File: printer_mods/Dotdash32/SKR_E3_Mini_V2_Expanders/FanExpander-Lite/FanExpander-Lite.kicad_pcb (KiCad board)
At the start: 2 copper layers, 35.1 x 34.7 mm, 31 parts, among them J1 FAN1, J2 FAN2, J3 FAN3, J4 FAN4, J5 EXP1_IN, J6 FAN1_IN, J7 IO_PassThrough, Q1 IRLML6344, Q2 IRLML6344, Q3 IRLML6344

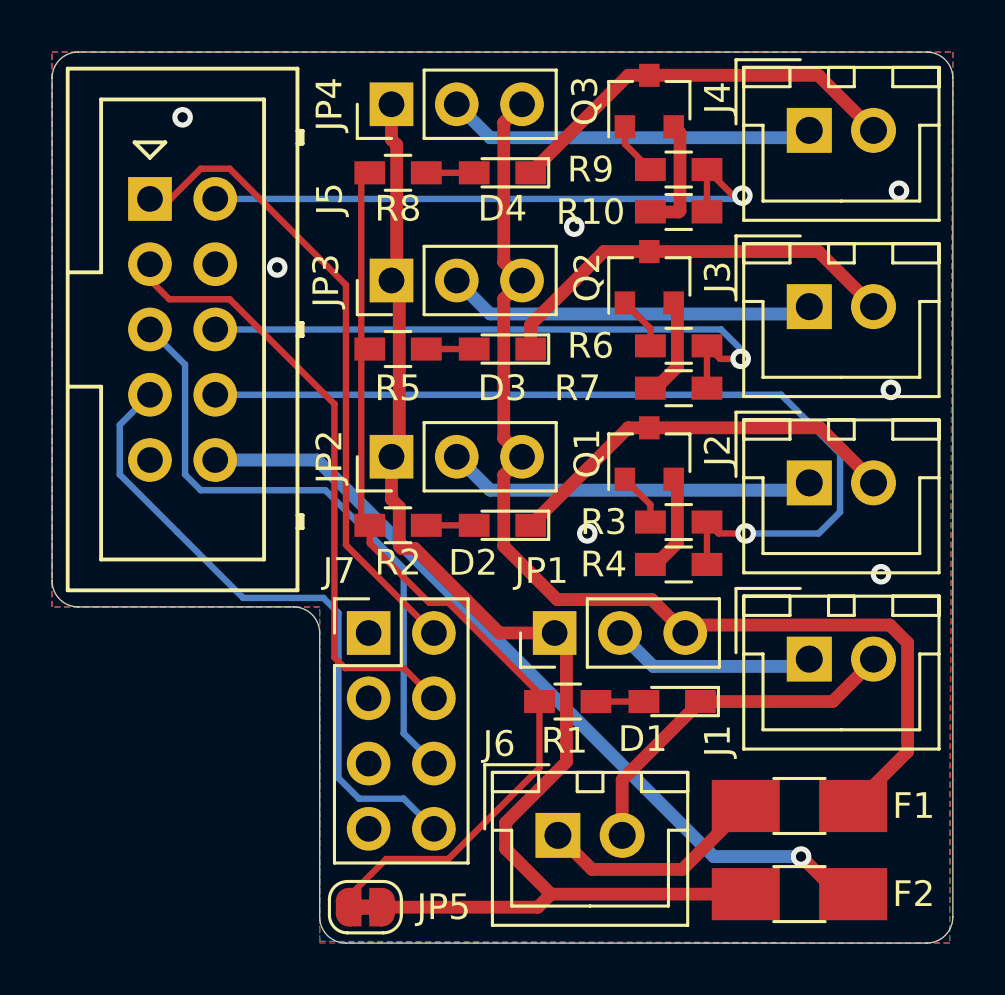
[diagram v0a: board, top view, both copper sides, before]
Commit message: feat: redo layout to use backside SMD parts
move to align with main board version, compactness!
Also moving to larger THT PTC fuses
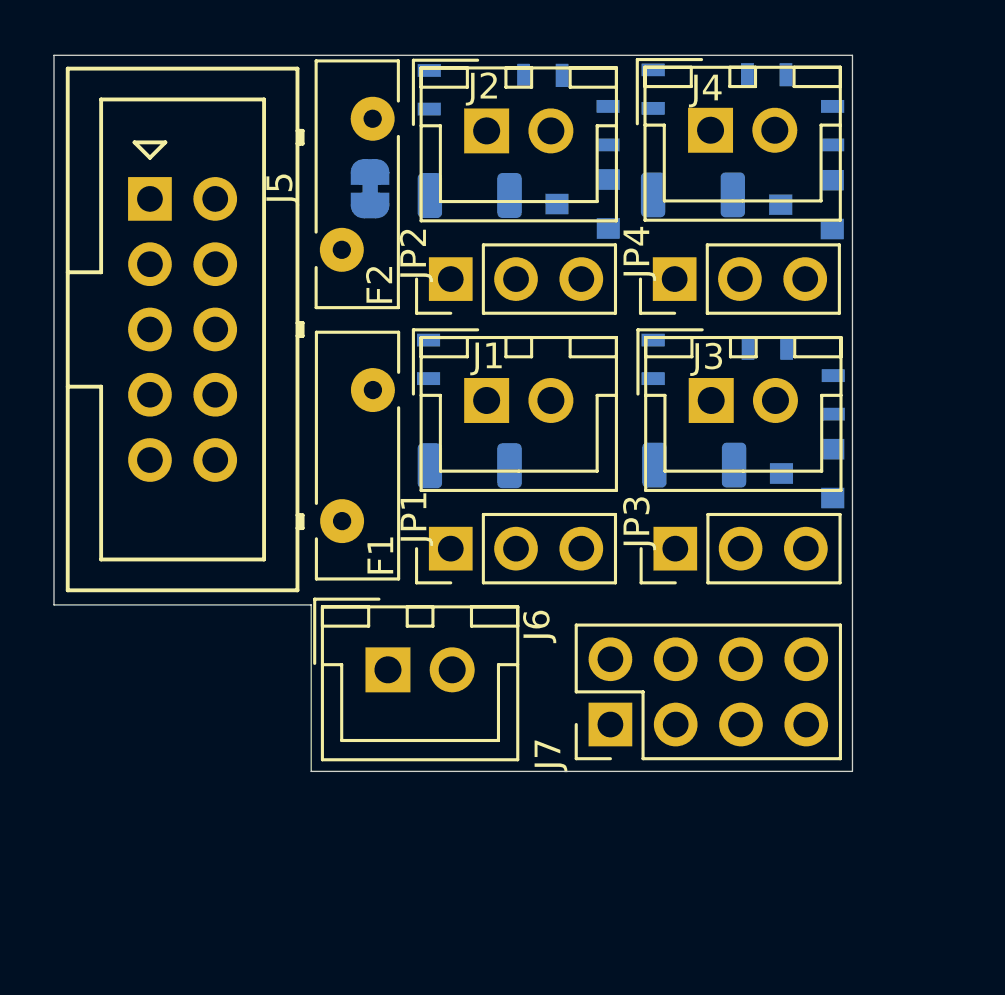
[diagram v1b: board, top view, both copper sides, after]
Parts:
- D1, D2, D3, D4: footprint LEDs:LED_0603_HandSoldering -> LED_SMD:LED_1206_3216Metric_ReverseMount_Hole1.8x2.4mm; moved to B.Cu
- F1: value Polyfuse-2A -> Polyfuse-3A; footprint Fuse_Holders_and_Fuses:Fuse_SMD1206_HandSoldering -> Fuse:Fuse_Bourns_MF-RHT200
- F2: footprint Fuse_Holders_and_Fuses:Fuse_SMD1206_HandSoldering -> Fuse:Fuse_Bourns_MF-RHT200
- JP5, Q1, Q2, Q3: moved to B.Cu
- R1, R10, R2, R3, R4, R5, R6, R7, R8, R9: footprint Resistors_SMD:R_0603_HandSoldering -> Resistors_SMD:R_0603; moved to B.Cu
- moved F2 34.4 mm to (52.1, 42.6), turned to 270 degrees
- moved JP5 28.0 mm to (52.0, 45.3), turned to 270 degrees
- moved F1 21.0 mm to (50.9, 58.3), turned to 90 degrees
- moved R4 19.8 mm to (58.7, 40.9)
- moved J2 18.6 mm to (56.5, 43.1)
- moved R2 17.0 mm to (54.3, 41.5), turned to 90 degrees
- moved J1 16.1 mm to (56.5, 53.6)
- moved R3 15.7 mm to (61.3, 42.9), turned to 90 degrees
- moved JP3 15.2 mm to (63.9, 59.3)
- moved R1 14.4 mm to (54.3, 52.0), turned to 270 degrees
- moved JP4 12.9 mm to (63.9, 48.8)
- moved D2 12.9 mm to (55.9, 45.6)
- moved D1 12.1 mm to (55.9, 56.1)
- moved R8 10.4 mm to (63.0, 41.4), turned to 90 degrees
- moved J7 10.1 mm to (61.4, 66.2), turned to 90 degrees
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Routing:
- net +5V: track 51.6 -> 0.00 mm
- net +24V: track 43.4 -> 0.00 mm
- net /LED_Drive: track 36.8 -> 0.00 mm
- net /FAN2: track 34.9 -> 0.00 mm, vias 1 -> 0
- net /5V_unFused: track 31.8 -> 0.00 mm, vias 1 -> 0
- net /PASS3: track 25.3 -> 0.00 mm
- net /PASS0: track 24.9 -> 0.00 mm
- net /FAN3: track 24.3 -> 0.00 mm, vias 1 -> 0
- net /PASS2: track 24.3 -> 0.00 mm
- net /PASS1: track 24.2 -> 0.00 mm
- net /FAN4: track 24.1 -> 0.00 mm, vias 1 -> 0
- net /FAN3_Drive: track 16.4 -> 0.00 mm
- net /FAN2_Drive: track 15.8 -> 0.00 mm
- net /FAN4_Drive: track 15.8 -> 0.00 mm
- net /F4V: track 14.4 -> 0.00 mm
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- removed copper zone on B.Cu, net GND
- removed copper zone on F.Cu, net GND
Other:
- board size 35.1 x 34.7 mm -> 31.1 x 27.9 mm
- board text removed: "5V F1 24V"
- board text removed: "5V F2 24V"
- board text removed: "5V F3 24V"
- board text removed: "5V F4 24V"
- board text removed: "Fan1 Pass"
- board text removed: "Fan2 PB15"
- board text removed: "Fan3 PB9"
- board text removed: "Fan4 PA15"
- board text removed: "PB8 PA10 PA0 PB5"

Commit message: feat: routing the board
no external 5V tap, but it'll probably be fine??
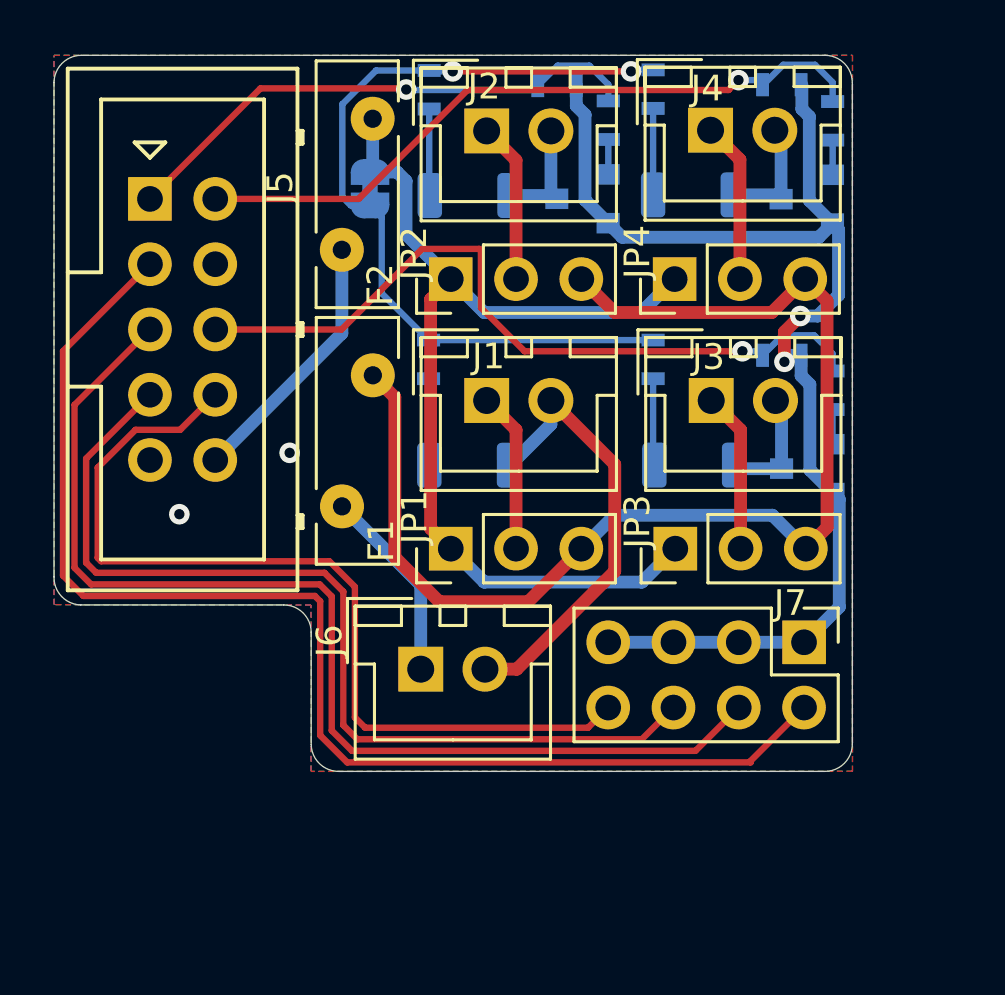
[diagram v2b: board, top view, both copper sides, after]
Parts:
- D1, D2, D3, D4: footprint LED_SMD:LED_1206_3216Metric_ReverseMount_Hole1.8x2.4mm -> LED_SMD:LED_1206_3216Metric_ReverseMount_Hole2.1x2.4mm
- F1: value Polyfuse-3A -> Polyfuse-2A
- F2: value Polyfuse-1A -> Polyfuse-2A
- moved J7 8.19 mm to (68.9, 63.0), turned to 270 degrees
- moved J6 1.28 mm to (54.0, 64.0)
- moved R10 0.70 mm to (68.0, 41.3), turned to 180 degrees
- moved R4 0.68 mm to (59.3, 41.3), turned to 0 degrees
- moved R7 0.63 mm to (68.0, 51.8), turned to 180 degrees
- moved F1 0.57 mm to (50.9, 57.7)
- moved Q3 0.21 mm to (69.0, 45.7)
- moved R3 0.21 mm to (61.3, 42.7)
- moved Q1 0.20 mm to (60.3, 45.7)
- moved Q2 0.19 mm to (69.0, 56.2)
- moved R9 0.19 mm to (70.0, 42.7)
- moved R6 0.18 mm to (70.0, 53.2)
- turned R1 to 90 degrees
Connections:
- J5 pad 1: /PASS0 -> /FAN2
- J5 pad 3: /PASS1 -> /PASS0
- J5 pad 5: /PASS2 -> /PASS1
- J5 pad 7: /PASS3 -> /PASS2
- J5 pad 8: /FAN2 -> /PASS3
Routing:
- net /PASS0: track 0.00 -> 49.3 mm
- net GND: track 0.00 -> 48.4 mm, vias 0 -> 4
- net +24V: track 0.00 -> 47.0 mm
- net /PASS1: track 0.00 -> 43.0 mm
- net +5V: track 0.00 -> 38.9 mm
- net /PASS2: track 0.00 -> 36.8 mm
- net /PASS3: track 0.00 -> 35.2 mm
- net /LED_Drive: track 0.00 -> 32.4 mm, vias 0 -> 2
- net /FAN3: track 0.00 -> 29.7 mm, vias 0 -> 1
- net /FAN4: track 0.00 -> 27.4 mm, vias 0 -> 1
- net /FAN2: track 0.00 -> 21.0 mm, vias 0 -> 1
- net /FAN1_Drive: track 0.00 -> 17.5 mm
- net /5V_unFused: track 0.00 -> 10.2 mm
- net /24V_unFused: track 0.00 -> 7.60 mm
- net /F4V: track 0.00 -> 6.26 mm
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- added copper zone on B.Cu, net GND
- added copper zone on F.Cu, net GND
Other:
- outline, holes or cut-outs redrawn
- board text added: "A9 A10 B8 B15"
- board text added: "LED EN"
- board text added: "SKR E3 Mini Fan Exp Lite"
- board text added: "by Dotdash32 (JDeW) 12/21"
- board text removed: "Designed by Dotdash32 (JDeW) 12/21"
- board text removed: "LED EN (over)"
- board text removed: "SKR E3 Mini Fan Expander Lite 1+3 Volt Select Fans 4 I/O Pins"

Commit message: feat: trim outline to not collide with TH exp
also some fun little changes for internal structure
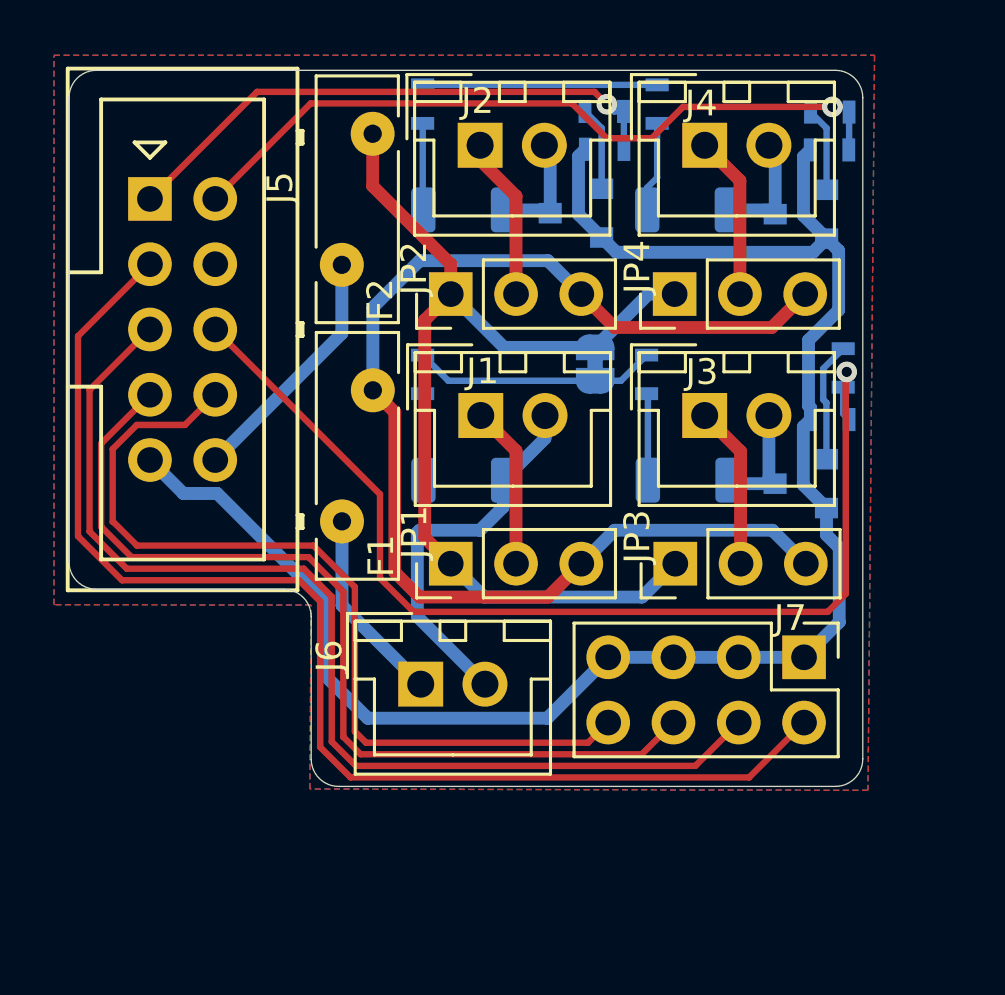
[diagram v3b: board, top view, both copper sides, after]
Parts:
- moved JP5 11.1 mm to (60.8, 52.1)
- moved R10 3.14 mm to (69.9, 43.8), turned to 0 degrees
- moved R7 3.12 mm to (69.9, 54.3), turned to 0 degrees
- moved R4 3.09 mm to (61.1, 43.8), turned to 180 degrees
- moved R6 0.95 mm to (70.4, 52.3), turned to 270 degrees
- moved D3 0.64 mm to (64.4, 56.7)
- moved J3 0.64 mm to (65.0, 54.1)
- moved Q2 0.64 mm to (68.8, 56.8)
- moved R5 0.64 mm to (62.8, 52.5)
- moved D1 0.63 mm to (55.6, 56.7)
- moved D4 0.63 mm to (64.3, 46.1)
- moved J1 0.63 mm to (56.3, 54.1)
- moved J4 0.63 mm to (65.0, 43.6)
- moved Q3 0.63 mm to (68.8, 46.3)
- moved R1 0.63 mm to (54.0, 52.5)
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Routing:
- net GND: track 48.4 -> 67.6 mm, vias 4 -> 0
- net /LED_Drive: track 32.4 -> 18.7 mm, vias 2 -> 0
- net /FAN3: track 29.7 -> 42.2 mm
- net Net-(Q2-Pad1): track 1.36 -> 4.67 mm
- net /FAN1_Drive: track 17.5 -> 15.0 mm
- net Net-(Q3-Pad1): track 1.35 -> 3.28 mm
- net Net-(Q1-Pad1): track 1.36 -> 3.28 mm
- net /FAN4: track 27.4 -> 28.8 mm
- net /PASS0: track 49.3 -> 48.1 mm
- net /PASS1: track 43.0 -> 41.9 mm
- net /PASS2: track 36.8 -> 35.7 mm
- net /PASS3: track 35.2 -> 34.2 mm
- net /FAN2: track 21.0 -> 21.9 mm
- net +24V: track 47.0 -> 47.9 mm
- net /5V_unFused: track 10.2 -> 9.64 mm
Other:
- board size 31.1 x 27.9 mm -> 30.9 x 27.9 mm
- board text added: "JLCJLCJLCJLC"
- board text added: "by Dotdash32 (JDeW) V1.0.1"
- board text removed: "by Dotdash32 (JDeW) 12/21"

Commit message: feat: add LCSC bom, add alignment fiducials
redoing some BOM stuff, oh how i hate BOM management
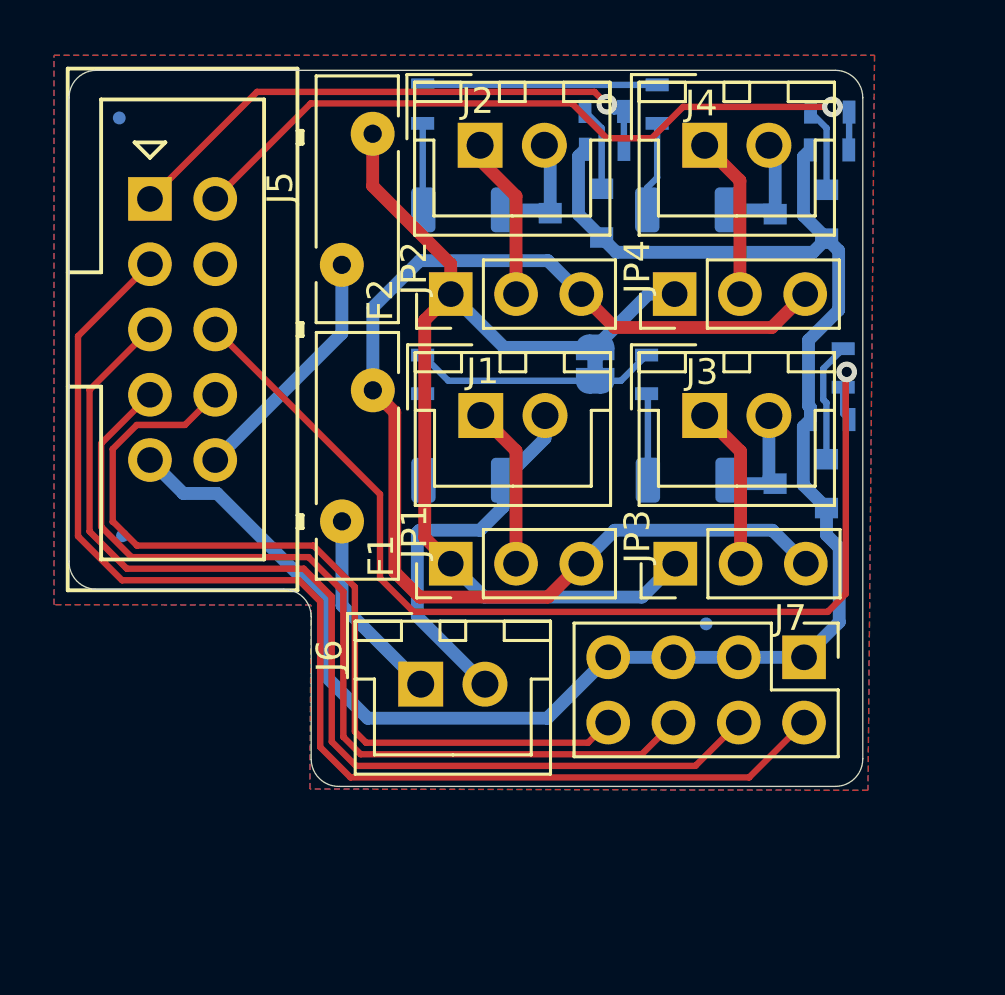
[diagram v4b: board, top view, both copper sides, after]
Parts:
- added FID1: Fiducial, Fiducials:Fiducial_0.5mm_Dia_1mm_Outer, B.Cu at (42.2, 42.6)
- added FID2: Fiducial, Fiducials:Fiducial_0.5mm_Dia_1mm_Outer, B.Cu at (42.4, 58.8)
- added FID3: Fiducial, Fiducials:Fiducial_0.5mm_Dia_1mm_Outer, B.Cu at (65.1, 62.3)
- D1, D2, D3, D4: footprint LED_SMD:LED_1206_3216Metric_ReverseMount_Hole2.1x2.4mm -> LED_SMD:LED_1206_3216Metric_ReverseMount_Hole1.8x2.4mm
- F1, F2: value Polyfuse-2A -> MF-RHT200/32
- J1: value FAN1 -> JST-XH2
- J2: value FAN2 -> JST-XH2
- J3: value FAN3 -> JST-XH2
- J4: value FAN4 -> JST-XH2
- J6: value FAN1_IN -> JST-XH2
- JP1: value V_SELECT1 -> V_SELECT
- JP2: value V_SELECT2 -> V_SELECT
- JP3: value V_SELECT3 -> V_SELECT
- JP4: value V_SELECT4 -> V_SELECT
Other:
- board text added: "by Dotdash32 (JDeW) V1.0.2"
- board text removed: "by Dotdash32 (JDeW) V1.0.1"

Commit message: fix: update reverse LED mounts at SCH level
were using the wrong hole pattern, not big enough!!
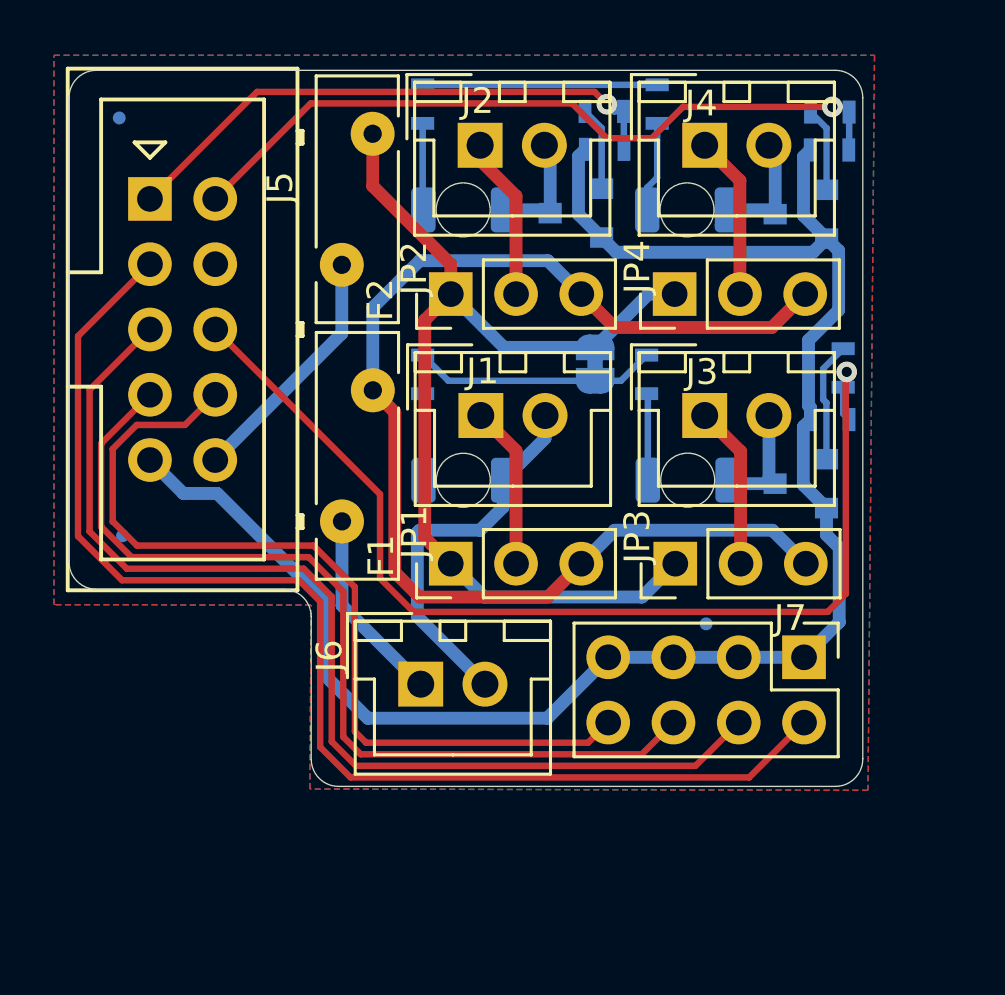
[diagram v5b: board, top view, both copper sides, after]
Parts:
- D1, D2, D3, D4: footprint LED_SMD:LED_1206_3216Metric_ReverseMount_Hole1.8x2.4mm -> LED_SMD:LED_1206_3216Metric_ReverseMount_Hole2.1x2.1mm
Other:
- board text added: "by Dotdash32 (JDeW) V1.0.3"
- board text removed: "by Dotdash32 (JDeW) V1.0.2"
